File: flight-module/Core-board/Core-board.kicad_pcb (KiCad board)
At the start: 4 copper layers, 127 x 95.2 mm, 28 parts, among them J1 POWER, J10 PCIE, J2 PCIE, J3 XT60-M, J4 PCIE, J5 PCIE, J6 ESP32-DEVKITC-32D, J7 Conn_01x19_Male, J8 PCIE, J9 Conn_01x19_Male, SW1 SW_SPST, U1 AZ1117IH-3.3TRG1, U2 74HC4050D, U3 XTSD04GLGEAG, U4 AZ1117IH-5TRG1

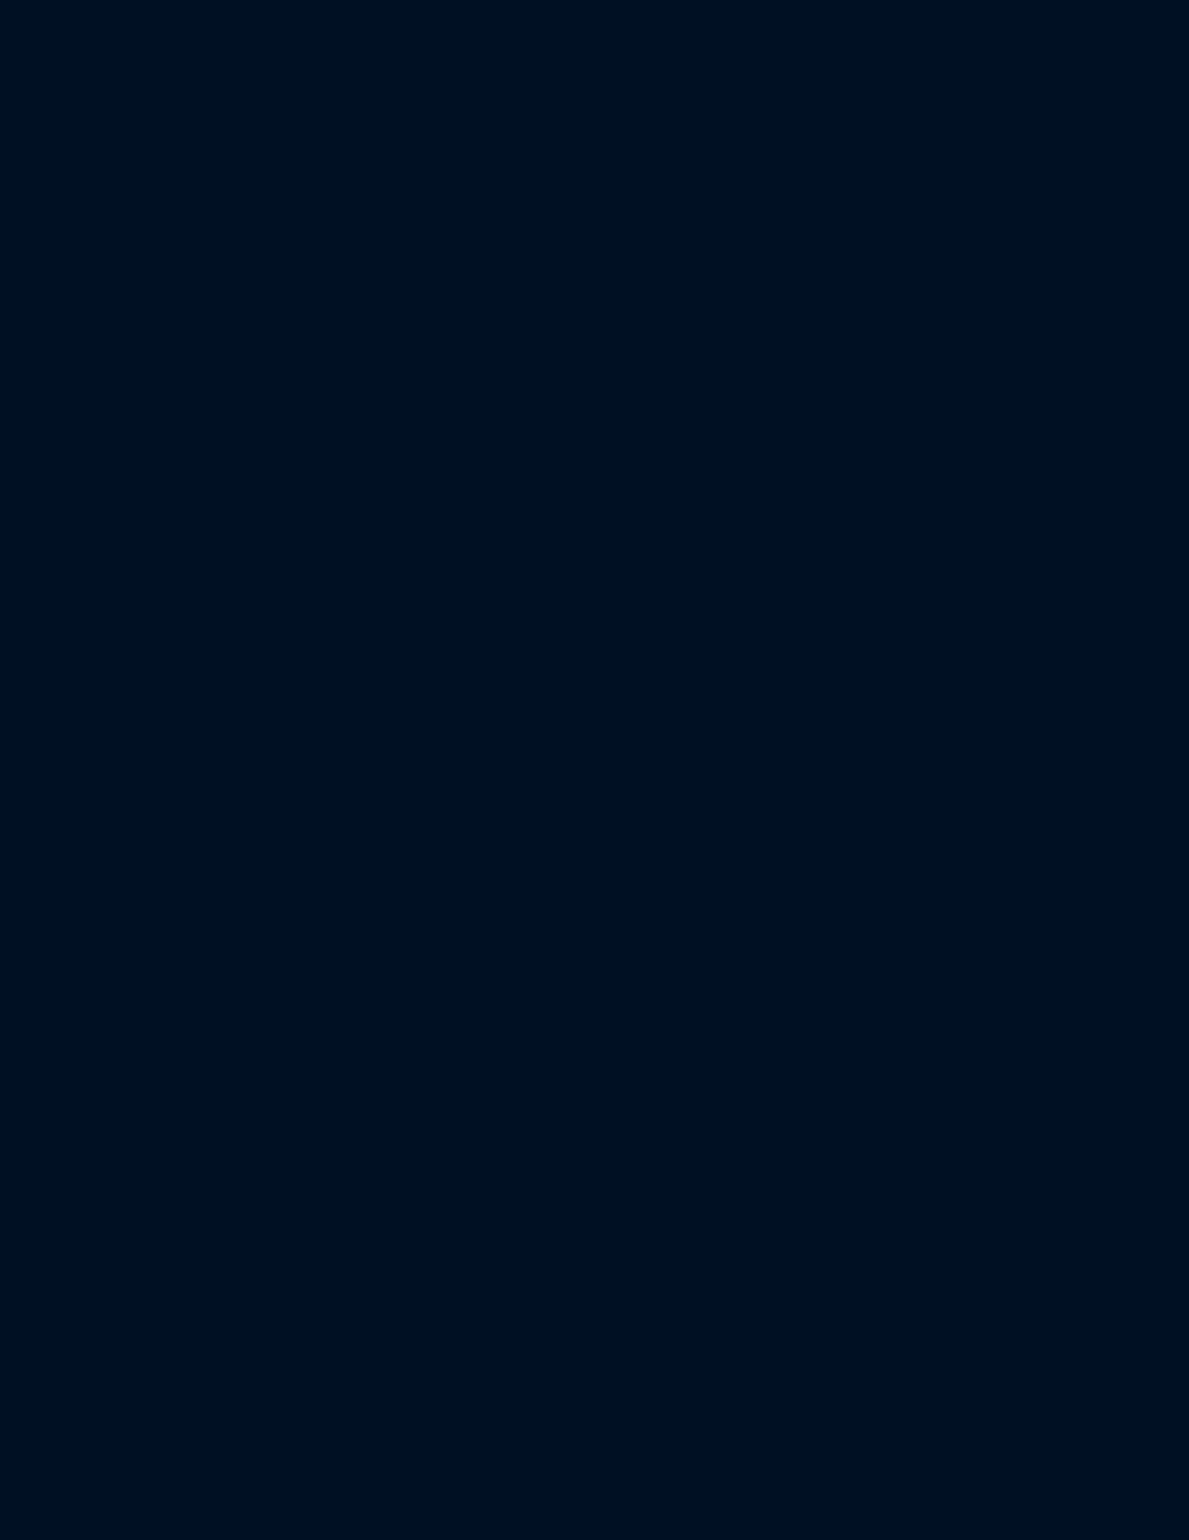
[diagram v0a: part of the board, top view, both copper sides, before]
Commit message: worked on core-board schematic. Not done.
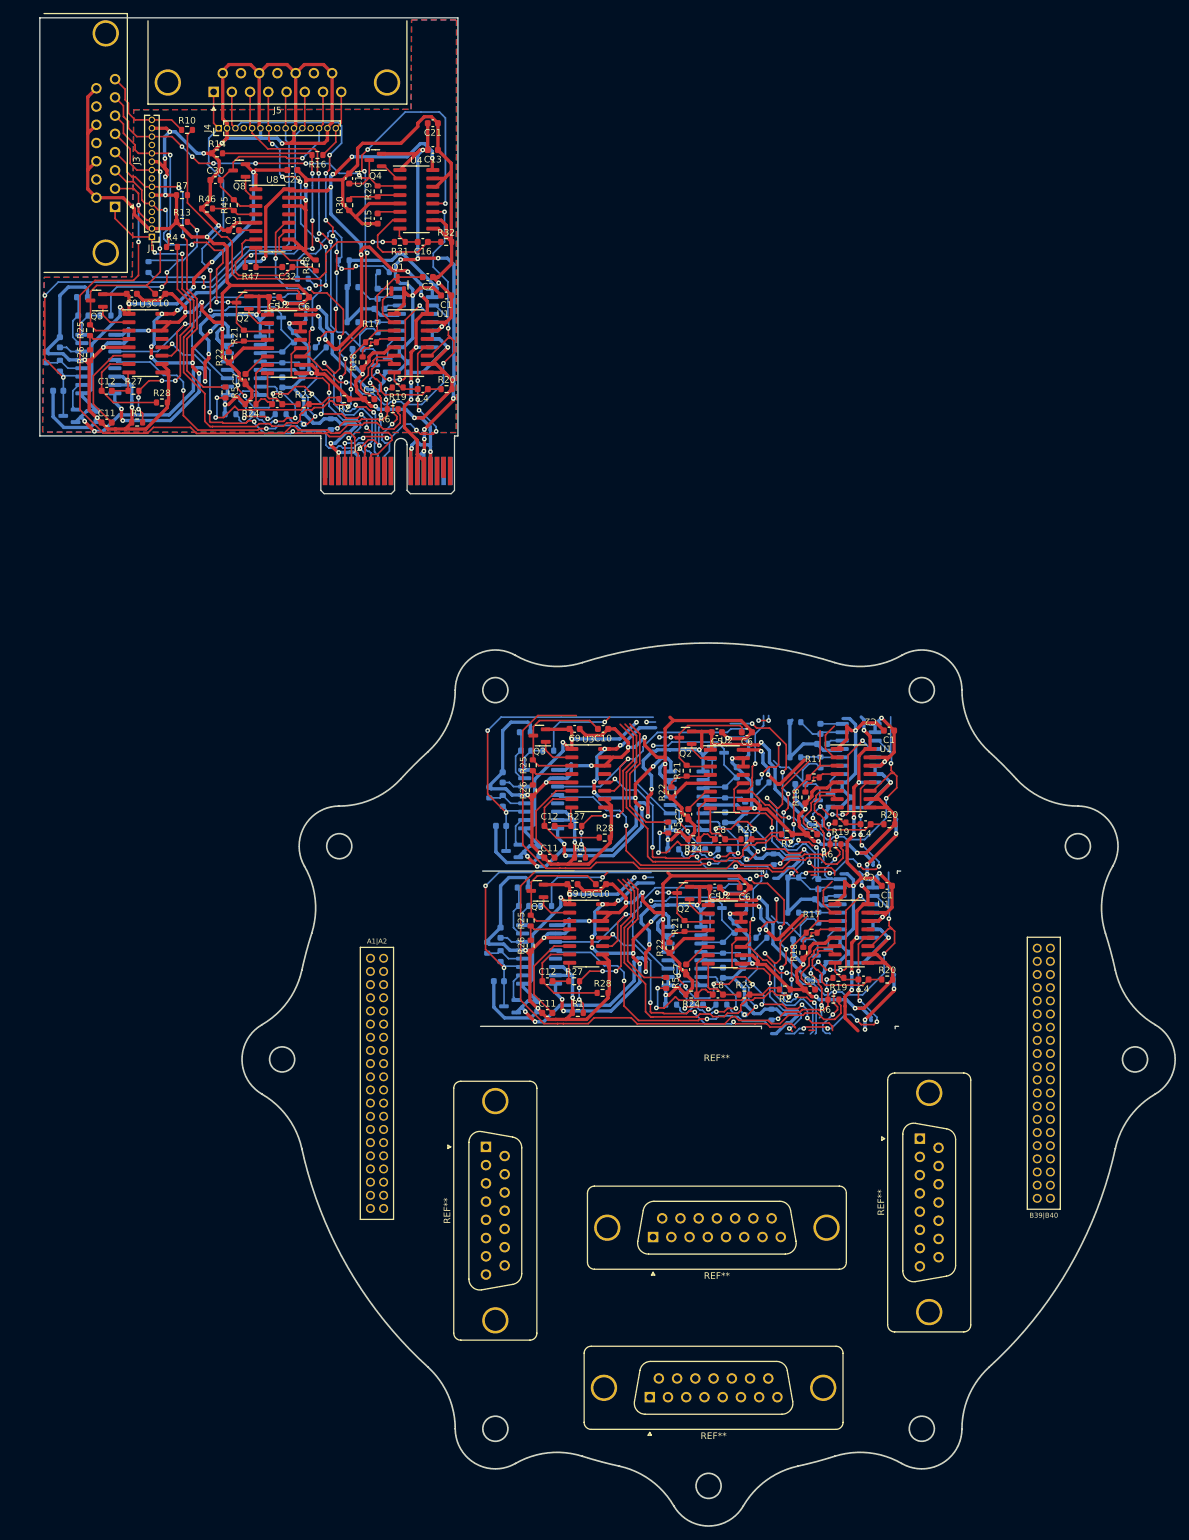
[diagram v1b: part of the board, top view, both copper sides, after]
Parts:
- added C1: 10uF, Capacitor_SMD:C_0603_1608Metric, F.Cu at (521.9, 120.1)
- added C1: 10uF, Capacitor_SMD:C_0603_1608Metric, F.Cu at (454.9, 30.4)
- added C1: 10uF, Capacitor_SMD:C_0603_1608Metric, F.Cu at (522.2, 96.5)
- added C10: 10uF, Capacitor_SMD:C_0603_1608Metric, F.Cu at (478.4, 119.8)
- added C10: 10uF, Capacitor_SMD:C_0603_1608Metric, F.Cu at (411.5, 30.1)
- added C10: 10uF, Capacitor_SMD:C_0603_1608Metric, F.Cu at (478.8, 96.2)
- added C11: 0.1uF, Capacitor_SMD:C_0603_1608Metric, F.Cu at (470.6, 115.8)
- added C11: 0.1uF, Capacitor_SMD:C_0603_1608Metric, F.Cu at (403.4, 49.7)
- added C11: 0.1uF, Capacitor_SMD:C_0603_1608Metric, F.Cu at (470.3, 139.4)
- added C12: 0.1uF, Capacitor_SMD:C_0603_1608Metric, F.Cu at (470.6, 111.0)
- added C12: 0.1uF, Capacitor_SMD:C_0603_1608Metric, F.Cu at (470.3, 134.5)
- added C12: 0.1uF, Capacitor_SMD:C_0603_1608Metric, F.Cu at (403.4, 44.9)
- added C13: 10uF, Capacitor_SMD:C_0603_1608Metric, F.Cu at (452.9, 8.29)
- added C14: 10uF, Capacitor_SMD:C_0603_1608Metric, F.Cu at (440.2, 12.6)
- added C15: 0.1uF, Capacitor_SMD:C_0603_1608Metric, F.Cu at (444.5, 18.7)
- added C16: 0.1uF, Capacitor_SMD:C_0603_1608Metric, F.Cu at (451.4, 22.3)
- added C17: 10uF, Capacitor_SMD:C_0603_1608Metric, B.Cu at (516.4, 107.4)
- added C17: 10uF, Capacitor_SMD:C_0603_1608Metric, B.Cu at (449.1, 41.3)
- added C17: 10uF, Capacitor_SMD:C_0603_1608Metric, B.Cu at (516.0, 131.0)
- added C18: 10uF, Capacitor_SMD:C_0603_1608Metric, B.Cu at (498.8, 126.4)
- added C18: 10uF, Capacitor_SMD:C_0603_1608Metric, B.Cu at (499.1, 102.8)
- added C18: 10uF, Capacitor_SMD:C_0603_1608Metric, B.Cu at (431.8, 36.8)
- added C19: 0.1uF, Capacitor_SMD:C_0603_1608Metric, B.Cu at (497.3, 109.7)
- added C19: 0.1uF, Capacitor_SMD:C_0603_1608Metric, B.Cu at (430.0, 43.6)
- added C19: 0.1uF, Capacitor_SMD:C_0603_1608Metric, B.Cu at (497.0, 133.3)
- added C2: 10uF, Capacitor_SMD:C_0603_1608Metric, F.Cu at (452.1, 27.6)
- added C20: 0.1uF, Capacitor_SMD:C_0603_1608Metric, B.Cu at (493.2, 138.1)
- added C20: 0.1uF, Capacitor_SMD:C_0603_1608Metric, B.Cu at (493.5, 114.5)
- added C20: 0.1uF, Capacitor_SMD:C_0603_1608Metric, B.Cu at (426.2, 48.4)
- added C21: 10uF, Capacitor_SMD:C_0603_1608Metric, F.Cu at (452.9, 4.23)
- added C22: 10uF, Capacitor_SMD:C_0603_1608Metric, B.Cu at (508.4, 128.2)
- added C22: 10uF, Capacitor_SMD:C_0603_1608Metric, B.Cu at (508.7, 104.6)
- added C22: 10uF, Capacitor_SMD:C_0603_1608Metric, B.Cu at (441.5, 38.5)
- added C23: 0.1uF, Capacitor_SMD:C_0603_1608Metric, B.Cu at (511.7, 122.1)
- added C23: 0.1uF, Capacitor_SMD:C_0603_1608Metric, B.Cu at (444.8, 32.4)
- added C23: 0.1uF, Capacitor_SMD:C_0603_1608Metric, B.Cu at (512.0, 98.5)
- added C24: 0.1uF, Capacitor_SMD:C_0603_1608Metric, B.Cu at (511.5, 119.8)
- added C24: 0.1uF, Capacitor_SMD:C_0603_1608Metric, B.Cu at (511.8, 96.2)
- added C24: 0.1uF, Capacitor_SMD:C_0603_1608Metric, B.Cu at (444.5, 30.1)
- added C25: 10uF, Capacitor_SMD:C_0603_1608Metric, B.Cu at (469.1, 114.8)
- added C25: 10uF, Capacitor_SMD:C_0603_1608Metric, B.Cu at (401.9, 48.7)
- added C25: 10uF, Capacitor_SMD:C_0603_1608Metric, B.Cu at (468.8, 138.4)
- added C26: 10uF, Capacitor_SMD:C_0603_1608Metric, B.Cu at (462.9, 134.5)
- added C26: 10uF, Capacitor_SMD:C_0603_1608Metric, B.Cu at (396.0, 44.9)
- added C26: 10uF, Capacitor_SMD:C_0603_1608Metric, B.Cu at (463.3, 111.0)
- added C27: 0.1uF, Capacitor_SMD:C_0603_1608Metric, B.Cu at (396.3, 37.5)
- added C27: 0.1uF, Capacitor_SMD:C_0603_1608Metric, B.Cu at (463.5, 103.6)
- added C27: 0.1uF, Capacitor_SMD:C_0603_1608Metric, B.Cu at (463.2, 127.2)
- added C28: 0.1uF, Capacitor_SMD:C_0603_1608Metric, B.Cu at (466.8, 123.1)
- added C28: 0.1uF, Capacitor_SMD:C_0603_1608Metric, B.Cu at (467.1, 99.5)
- added C28: 0.1uF, Capacitor_SMD:C_0603_1608Metric, B.Cu at (399.8, 33.4)
- added C29: 10uF, Capacitor_SMD:C_0603_1608Metric, F.Cu at (431.6, 11.3)
- added C3: 0.1uF, Capacitor_SMD:C_0603_1608Metric, F.Cu at (443.3, 46.1)
- added C3: 0.1uF, Capacitor_SMD:C_0603_1608Metric, F.Cu at (510.2, 135.8)
- added C3: 0.1uF, Capacitor_SMD:C_0603_1608Metric, F.Cu at (510.5, 112.2)
- added C30: 10uF, Capacitor_SMD:C_0603_1608Metric, F.Cu at (419.9, 12.9)
- added C31: 0.1uF, Capacitor_SMD:C_0603_1608Metric, F.Cu at (422.7, 20.5)
- added C32: 0.1uF, Capacitor_SMD:C_0603_1608Metric, F.Cu at (430.8, 26.1)
- added C4: 0.1uF, Capacitor_SMD:C_0603_1608Metric, F.Cu at (518.6, 110.7)
- added C4: 0.1uF, Capacitor_SMD:C_0603_1608Metric, F.Cu at (451.4, 44.6)
- added C4: 0.1uF, Capacitor_SMD:C_0603_1608Metric, F.Cu at (518.3, 134.3)
- added C5: 10uF, Capacitor_SMD:C_0603_1608Metric, F.Cu at (496.0, 96.7)
- added C5: 10uF, Capacitor_SMD:C_0603_1608Metric, F.Cu at (495.7, 120.3)
- added C5: 10uF, Capacitor_SMD:C_0603_1608Metric, F.Cu at (428.8, 30.6)
- added C6: 10uF, Capacitor_SMD:C_0603_1608Metric, F.Cu at (433.4, 30.6)
- added C6: 10uF, Capacitor_SMD:C_0603_1608Metric, F.Cu at (500.6, 96.7)
- added C6: 10uF, Capacitor_SMD:C_0603_1608Metric, F.Cu at (500.3, 120.3)
- added C7: 0.1uF, Capacitor_SMD:C_0603_1608Metric, F.Cu at (491.4, 132.8)
- added C7: 0.1uF, Capacitor_SMD:C_0603_1608Metric, F.Cu at (424.5, 43.1)
- added C7: 0.1uF, Capacitor_SMD:C_0603_1608Metric, F.Cu at (491.7, 109.2)
- added C8: 0.1uF, Capacitor_SMD:C_0603_1608Metric, F.Cu at (429.3, 46.9)
- added C8: 0.1uF, Capacitor_SMD:C_0603_1608Metric, F.Cu at (496.2, 136.6)
- added C8: 0.1uF, Capacitor_SMD:C_0603_1608Metric, F.Cu at (496.5, 113.0)
- added C9: 10uF, Capacitor_SMD:C_0603_1608Metric, F.Cu at (474.1, 119.8)
- added C9: 10uF, Capacitor_SMD:C_0603_1608Metric, F.Cu at (474.4, 96.2)
- added C9: 10uF, Capacitor_SMD:C_0603_1608Metric, F.Cu at (407.2, 30.1)
- added J1: Testpoints, Connector_PinHeader_1.27mm:PinHeader_1x15_P1.27mm_Vertical, F.Cu at (410.2, 21.5)
- added J2: PCIE-LP-01-01-F-DV-A-TR, Connector_PCBEdge:BUS_PCIexpress_x1, F.Cu at (436.6, 57.0)
- added J3: DB15_Female, DSUB_622-015-260-042:DSUB_622-015-260-042, F.Cu at (404.6, 16.9)
- added J4: Testpoints, Connector_PinHeader_1.27mm:PinHeader_1x15_P1.27mm_Vertical, F.Cu at (420.4, 4.99)
- added J5: DB15_Female, DSUB_622-015-260-042:DSUB_622-015-260-042, F.Cu at (419.6, -0.53)
- added Q1: MMBT4403LT3G, Package_TO_SOT_SMD:SOT-23, F.Cu at (447.6, 28.8)
- added Q2: MMBT4403LT3G, Package_TO_SOT_SMD:SOT-23, F.Cu at (491.0, 121.1)
- added Q2: MMBT4403LT3G, Package_TO_SOT_SMD:SOT-23, F.Cu at (424.0, 31.5)
- added Q2: MMBT4403LT3G, Package_TO_SOT_SMD:SOT-23, F.Cu at (491.3, 97.6)
- added Q3: MMBT4403LT3G, Package_TO_SOT_SMD:SOT-23, F.Cu at (401.9, 31.2)
- added Q3: MMBT4403LT3G, Package_TO_SOT_SMD:SOT-23, F.Cu at (469.1, 97.2)
- added Q3: MMBT4403LT3G, Package_TO_SOT_SMD:SOT-23, F.Cu at (468.8, 120.8)
- added Q4: MMBT4403LT3G, Package_TO_SOT_SMD:SOT-23, F.Cu at (444.2, 9.82)
- added Q5: MMBT4403LT3G, Package_TO_SOT_SMD:SOT-23, B.Cu at (496.2, 99.8)
- added Q5: MMBT4403LT3G, Package_TO_SOT_SMD:SOT-23, B.Cu at (429.0, 33.8)
- added Q5: MMBT4403LT3G, Package_TO_SOT_SMD:SOT-23, B.Cu at (495.9, 123.4)
- added Q6: MMBT4403LT3G, Package_TO_SOT_SMD:SOT-23, B.Cu at (445.1, 41.0)
- added Q6: MMBT4403LT3G, Package_TO_SOT_SMD:SOT-23, B.Cu at (512.4, 107.1)
- added Q6: MMBT4403LT3G, Package_TO_SOT_SMD:SOT-23, B.Cu at (512.0, 130.7)
- added Q7: MMBT4403LT3G, Package_TO_SOT_SMD:SOT-23, B.Cu at (464.6, 138.4)
- added Q7: MMBT4403LT3G, Package_TO_SOT_SMD:SOT-23, B.Cu at (397.7, 48.7)
- added Q7: MMBT4403LT3G, Package_TO_SOT_SMD:SOT-23, B.Cu at (465.0, 114.8)
- added Q8: MMBT4403LT3G, Package_TO_SOT_SMD:SOT-23, F.Cu at (423.5, 11.4)
- added R1: 2kΩ, Resistor_SMD:R_0603_1608Metric, F.Cu at (475.3, 115.8)
- added R1: 2kΩ, Resistor_SMD:R_0603_1608Metric, F.Cu at (474.9, 139.4)
- added R1: 2kΩ, Resistor_SMD:R_0603_1608Metric, F.Cu at (408.0, 49.7)
- added R10: 100kΩ, Resistor_SMD:R_0603_1608Metric, F.Cu at (415.6, 5.25)
- added R11: 100kΩ, Resistor_SMD:R_0603_1608Metric, B.Cu at (433.2, 27.9)
- added R12: 100kΩ, Resistor_SMD:R_0603_1608Metric, B.Cu at (503.1, 104.3)
- added R12: 100kΩ, Resistor_SMD:R_0603_1608Metric, B.Cu at (435.9, 38.3)
- added R12: 100kΩ, Resistor_SMD:R_0603_1608Metric, B.Cu at (502.8, 127.9)
- added R13: 2kΩ, Resistor_SMD:R_0603_1608Metric, F.Cu at (414.8, 19.2)
- added R14: 2kΩ, Resistor_SMD:R_0603_1608Metric, F.Cu at (420.1, 8.80)
- added R15: 100kΩ, Resistor_SMD:R_0603_1608Metric, B.Cu at (409.7, 26.1)
- added R16: 100kΩ, Resistor_SMD:R_0603_1608Metric, F.Cu at (435.4, 9.06)
- added R17: 20kΩ, Resistor_SMD:R_0603_1608Metric, F.Cu at (443.5, 37.5)
- added R17: 20kΩ, Resistor_SMD:R_0603_1608Metric, F.Cu at (510.8, 103.6)
- added R17: 20kΩ, Resistor_SMD:R_0603_1608Metric, F.Cu at (510.4, 127.2)
- added R18: 8.2kΩ, Resistor_SMD:R_0603_1608Metric, F.Cu at (509.5, 106.6)
- added R18: 8.2kΩ, Resistor_SMD:R_0603_1608Metric, F.Cu at (442.2, 40.6)
- added R18: 8.2kΩ, Resistor_SMD:R_0603_1608Metric, F.Cu at (509.2, 130.2)
- added R19: 100Ω, Resistor_SMD:R_0603_1608Metric, F.Cu at (514.8, 110.4)
- added R19: 100Ω, Resistor_SMD:R_0603_1608Metric, F.Cu at (514.5, 134.0)
- added R19: 100Ω, Resistor_SMD:R_0603_1608Metric, F.Cu at (447.6, 44.4)
- added R2: 2kΩ, Resistor_SMD:R_0603_1608Metric, F.Cu at (506.7, 112.2)
- added R2: 2kΩ, Resistor_SMD:R_0603_1608Metric, F.Cu at (439.4, 46.1)
- added R2: 2kΩ, Resistor_SMD:R_0603_1608Metric, F.Cu at (506.4, 135.8)
- added R20: 100Ω, Resistor_SMD:R_0603_1608Metric, F.Cu at (521.9, 134.3)
- added R20: 100Ω, Resistor_SMD:R_0603_1608Metric, F.Cu at (455.0, 44.6)
- added R20: 100Ω, Resistor_SMD:R_0603_1608Metric, F.Cu at (522.2, 110.7)
- added R21: 20kΩ, Resistor_SMD:R_0603_1608Metric, F.Cu at (491.5, 102.6)
- added R21: 20kΩ, Resistor_SMD:R_0603_1608Metric, F.Cu at (491.1, 126.2)
- added R21: 20kΩ, Resistor_SMD:R_0603_1608Metric, F.Cu at (424.2, 36.5)
- added R22: 8.2kΩ, Resistor_SMD:R_0603_1608Metric, F.Cu at (421.9, 39.8)
- added R22: 8.2kΩ, Resistor_SMD:R_0603_1608Metric, F.Cu at (489.2, 105.9)
- added R22: 8.2kΩ, Resistor_SMD:R_0603_1608Metric, F.Cu at (488.9, 129.5)
- added R23: 100Ω, Resistor_SMD:R_0603_1608Metric, F.Cu at (500.2, 136.6)
- added R23: 100Ω, Resistor_SMD:R_0603_1608Metric, F.Cu at (433.3, 46.9)
- added R23: 100Ω, Resistor_SMD:R_0603_1608Metric, F.Cu at (500.5, 113.0)
- added R24: 100Ω, Resistor_SMD:R_0603_1608Metric, F.Cu at (492.2, 136.6)
- added R24: 100Ω, Resistor_SMD:R_0603_1608Metric, F.Cu at (425.2, 46.9)
- added R24: 100Ω, Resistor_SMD:R_0603_1608Metric, F.Cu at (492.5, 113.0)
- added R25: 20kΩ, Resistor_SMD:R_0603_1608Metric, F.Cu at (400.8, 35.7)
- added R25: 20kΩ, Resistor_SMD:R_0603_1608Metric, F.Cu at (468.1, 101.7)
- added R25: 20kΩ, Resistor_SMD:R_0603_1608Metric, F.Cu at (467.8, 125.3)
- added R26: 8.2kΩ, Resistor_SMD:R_0603_1608Metric, F.Cu at (400.8, 39.5)
- added R26: 8.2kΩ, Resistor_SMD:R_0603_1608Metric, F.Cu at (468.1, 105.6)
- added R26: 8.2kΩ, Resistor_SMD:R_0603_1608Metric, F.Cu at (467.8, 129.1)
- added R27: 100Ω, Resistor_SMD:R_0603_1608Metric, F.Cu at (474.4, 134.5)
- added R27: 100Ω, Resistor_SMD:R_0603_1608Metric, F.Cu at (474.7, 111.0)
- added R27: 100Ω, Resistor_SMD:R_0603_1608Metric, F.Cu at (407.4, 44.9)
- added R28: 100Ω, Resistor_SMD:R_0603_1608Metric, F.Cu at (411.8, 46.6)
- added R28: 100Ω, Resistor_SMD:R_0603_1608Metric, F.Cu at (479.0, 112.7)
- added R28: 100Ω, Resistor_SMD:R_0603_1608Metric, F.Cu at (478.7, 136.3)
- added R29: 20kΩ, Resistor_SMD:R_0603_1608Metric, F.Cu at (444.5, 14.6)
- added R3: 2kΩ, Resistor_SMD:R_0603_1608Metric, B.Cu at (437.4, 50.0)
- added R3: 2kΩ, Resistor_SMD:R_0603_1608Metric, B.Cu at (504.7, 116.0)
- added R3: 2kΩ, Resistor_SMD:R_0603_1608Metric, B.Cu at (504.3, 139.6)
- added R30: 8.2kΩ, Resistor_SMD:R_0603_1608Metric, F.Cu at (440.2, 16.7)
- added R31: 100Ω, Resistor_SMD:R_0603_1608Metric, F.Cu at (447.9, 22.3)
- added R32: 100Ω, Resistor_SMD:R_0603_1608Metric, F.Cu at (454.9, 22.3)
- added R33: 20kΩ, Resistor_SMD:R_0603_1608Metric, B.Cu at (497.0, 129.5)
- added R33: 20kΩ, Resistor_SMD:R_0603_1608Metric, B.Cu at (430.0, 39.8)
- added R33: 20kΩ, Resistor_SMD:R_0603_1608Metric, B.Cu at (497.3, 105.9)
- added R34: 8.2kΩ, Resistor_SMD:R_0603_1608Metric, B.Cu at (433.1, 42.1)
- added R34: 8.2kΩ, Resistor_SMD:R_0603_1608Metric, B.Cu at (500.4, 108.2)
- added R34: 8.2kΩ, Resistor_SMD:R_0603_1608Metric, B.Cu at (500.0, 131.7)
- added R35: 100Ω, Resistor_SMD:R_0603_1608Metric, B.Cu at (429.8, 48.4)
- added R35: 100Ω, Resistor_SMD:R_0603_1608Metric, B.Cu at (496.7, 138.1)
- added R35: 100Ω, Resistor_SMD:R_0603_1608Metric, B.Cu at (497.0, 114.5)
- added R36: 100Ω, Resistor_SMD:R_0603_1608Metric, B.Cu at (489.4, 114.5)
- added R36: 100Ω, Resistor_SMD:R_0603_1608Metric, B.Cu at (422.2, 48.4)
- added R36: 100Ω, Resistor_SMD:R_0603_1608Metric, B.Cu at (489.1, 138.1)
- added R37: 20kΩ, Resistor_SMD:R_0603_1608Metric, B.Cu at (444.5, 35.2)
- added R37: 20kΩ, Resistor_SMD:R_0603_1608Metric, B.Cu at (511.5, 124.9)
- added R37: 20kΩ, Resistor_SMD:R_0603_1608Metric, B.Cu at (511.8, 101.3)
- added R38: 8.2kΩ, Resistor_SMD:R_0603_1608Metric, B.Cu at (507.6, 124.1)
- added R38: 8.2kΩ, Resistor_SMD:R_0603_1608Metric, B.Cu at (440.7, 34.5)
- added R38: 8.2kΩ, Resistor_SMD:R_0603_1608Metric, B.Cu at (508.0, 100.5)
- added R39: 100Ω, Resistor_SMD:R_0603_1608Metric, B.Cu at (445.5, 26.8)
- added R4: 100kΩ, Resistor_SMD:R_0603_1608Metric, F.Cu at (413.3, 23.0)
- added R40: 100Ω, Resistor_SMD:R_0603_1608Metric, B.Cu at (507.6, 118.8)
- added R40: 100Ω, Resistor_SMD:R_0603_1608Metric, B.Cu at (440.7, 29.1)
- added R40: 100Ω, Resistor_SMD:R_0603_1608Metric, B.Cu at (508.0, 95.2)
- added R41: 20kΩ, Resistor_SMD:R_0603_1608Metric, B.Cu at (463.2, 130.7)
- added R41: 20kΩ, Resistor_SMD:R_0603_1608Metric, B.Cu at (396.3, 41.1)
- added R41: 20kΩ, Resistor_SMD:R_0603_1608Metric, B.Cu at (463.5, 107.1)
- added R42: 8.2kΩ, Resistor_SMD:R_0603_1608Metric, B.Cu at (461.2, 129.5)
- added R42: 8.2kΩ, Resistor_SMD:R_0603_1608Metric, B.Cu at (461.5, 105.9)
- added R42: 8.2kΩ, Resistor_SMD:R_0603_1608Metric, B.Cu at (394.2, 39.8)
- added R43: 100Ω, Resistor_SMD:R_0603_1608Metric, B.Cu at (470.4, 99.5)
- added R43: 100Ω, Resistor_SMD:R_0603_1608Metric, B.Cu at (470.1, 123.1)
- added R43: 100Ω, Resistor_SMD:R_0603_1608Metric, B.Cu at (403.2, 33.4)
- added R44: 100Ω, Resistor_SMD:R_0603_1608Metric, B.Cu at (399.6, 30.6)
- added R44: 100Ω, Resistor_SMD:R_0603_1608Metric, B.Cu at (466.6, 120.3)
- added R44: 100Ω, Resistor_SMD:R_0603_1608Metric, B.Cu at (466.9, 96.7)
- added R45: 20kΩ, Resistor_SMD:R_0603_1608Metric, F.Cu at (422.7, 16.7)
- added R46: 8.2kΩ, Resistor_SMD:R_0603_1608Metric, F.Cu at (418.6, 17.2)
- added R47: 100Ω, Resistor_SMD:R_0603_1608Metric, F.Cu at (425.2, 26.1)
- added R48: 100Ω, Resistor_SMD:R_0603_1608Metric, F.Cu at (435.1, 25.8)
- added R5: 100kΩ, Resistor_SMD:R_0603_1608Metric, F.Cu at (488.3, 134.8)
- added R5: 100kΩ, Resistor_SMD:R_0603_1608Metric, F.Cu at (488.7, 111.2)
- added R5: 100kΩ, Resistor_SMD:R_0603_1608Metric, F.Cu at (421.4, 45.1)
- added R6: 100kΩ, Resistor_SMD:R_0603_1608Metric, F.Cu at (513.7, 137.3)
- added R6: 100kΩ, Resistor_SMD:R_0603_1608Metric, F.Cu at (446.8, 47.7)
- added R6: 100kΩ, Resistor_SMD:R_0603_1608Metric, F.Cu at (514.1, 113.7)
- added R7: 2kΩ, Resistor_SMD:R_0603_1608Metric, F.Cu at (414.8, 15.2)
- added R8: 2kΩ, Resistor_SMD:R_0603_1608Metric, B.Cu at (439.4, 25.1)
- added R9: 2kΩ, Resistor_SMD:R_0603_1608Metric, B.Cu at (433.3, 49.1)
- added R9: 2kΩ, Resistor_SMD:R_0603_1608Metric, B.Cu at (500.6, 115.2)
- added R9: 2kΩ, Resistor_SMD:R_0603_1608Metric, B.Cu at (500.2, 138.8)
- added REF**: DSUB-15_Female_Vertical_P2.77x2.84mm_MountingHoles, Connector_Dsub:DSUB-15_Female_Vertical_P2.77x2.84mm_MountingHoles, F.Cu at (461.0, 159.7)
- added REF**: DSUB-15_Female_Vertical_P2.77x2.84mm_MountingHoles, Connector_Dsub:DSUB-15_Female_Vertical_P2.77x2.84mm_MountingHoles, F.Cu at (486.4, 173.4)
- added REF**: Stack_Shape, Stack_Shape:Stack_Shape, F.Cu at (495.8, 147.6)
- added REF**: DSUB-15_Female_Vertical_P2.77x2.84mm_MountingHoles, Connector_Dsub:DSUB-15_Female_Vertical_P2.77x2.84mm_MountingHoles, F.Cu at (485.9, 197.7)
- added REF**: DSUB-15_Female_Vertical_P2.77x2.84mm_MountingHoles, Connector_Dsub:DSUB-15_Female_Vertical_P2.77x2.84mm_MountingHoles, F.Cu at (526.9, 158.5)
- added U1: HX711, Package_SO:SOP-16_3.9x9.9mm_P1.27mm, F.Cu at (516.5, 127.3)
- added U1: HX711, Package_SO:SOP-16_3.9x9.9mm_P1.27mm, F.Cu at (516.8, 103.7)
- added U1: HX711, Package_SO:SOP-16_3.9x9.9mm_P1.27mm, F.Cu at (449.6, 37.6)
- added U2: HX711, Package_SO:SOP-16_3.9x9.9mm_P1.27mm, F.Cu at (497.2, 127.4)
- added U2: HX711, Package_SO:SOP-16_3.9x9.9mm_P1.27mm, F.Cu at (497.6, 103.8)
- added U2: HX711, Package_SO:SOP-16_3.9x9.9mm_P1.27mm, F.Cu at (430.3, 37.8)
- added U3: HX711, Package_SO:SOP-16_3.9x9.9mm_P1.27mm, F.Cu at (476.2, 127.3)
- added U3: HX711, Package_SO:SOP-16_3.9x9.9mm_P1.27mm, F.Cu at (476.5, 103.7)
- added U3: HX711, Package_SO:SOP-16_3.9x9.9mm_P1.27mm, F.Cu at (409.3, 37.6)
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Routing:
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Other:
- board size 127 x 95.2 mm -> 310.1 x 163.5 mm
- board text added: "100kΩ"
- board text added: "C2"
- board text added: "MMBT4403LT3G"
- board text added: "PCIE-LP-01-01-F-DV-A-TR"
- board text added: "Q1"

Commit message: Progress on core board.
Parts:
- removed the C1 at (302.2, 132.5)
- removed the C1 at (521.9, 120.1)
- removed the C1 at (454.9, 30.4)
- removed the C1 at (522.2, 96.5)
- removed the C10 at (478.4, 119.8)
- removed the C10 at (411.5, 30.1)
- removed the C10 at (478.8, 96.2)
- removed the C11 at (470.6, 115.8)
- removed the C11 at (403.4, 49.7)
- removed the C11 at (470.3, 139.4)
- removed the C12 at (470.6, 111.0)
- removed the C12 at (470.3, 134.5)
- removed the C12 at (403.4, 44.9)
- removed the C17 at (516.4, 107.4)
- removed the C17 at (449.1, 41.3)
- removed the C17 at (516.0, 131.0)
- removed the C18 at (498.8, 126.4)
- removed the C18 at (499.1, 102.8)
- removed the C18 at (431.8, 36.8)
- removed the C19 at (497.3, 109.7)
- removed the C19 at (430.0, 43.6)
- removed the C19 at (497.0, 133.3)
- removed the C2 at (452.1, 27.6)
- removed the C2 at (306.2, 136.3)
- removed the C20 at (493.2, 138.1)
- removed the C20 at (493.5, 114.5)
- removed the C20 at (426.2, 48.4)
- removed the C22 at (508.4, 128.2)
- removed the C22 at (508.7, 104.6)
- removed the C22 at (441.5, 38.5)
- removed the C23 at (511.7, 122.1)
- removed the C23 at (444.8, 32.4)
- removed the C23 at (512.0, 98.5)
- removed the C24 at (511.5, 119.8)
- removed the C24 at (511.8, 96.2)
- removed the C24 at (444.5, 30.1)
- removed the C25 at (469.1, 114.8)
- removed the C25 at (401.9, 48.7)
- removed the C25 at (468.8, 138.4)
- removed the C26 at (462.9, 134.5)
- removed the C26 at (396.0, 44.9)
- removed the C26 at (463.3, 111.0)
- removed the C27 at (396.3, 37.5)
- removed the C27 at (463.5, 103.6)
- removed the C27 at (463.2, 127.2)
- removed the C28 at (466.8, 123.1)
- removed the C28 at (467.1, 99.5)
- removed the C28 at (399.8, 33.4)
- removed C29, C30: 10uF, Capacitor_SMD:C_0603_1608Metric
- removed the C3 at (301.6, 144.4)
- removed the C3 at (443.3, 46.1)
- removed the C3 at (510.2, 135.8)
- removed the C3 at (510.5, 112.2)
- removed C31, C32: 0.1uF, Capacitor_SMD:C_0603_1608Metric
- removed the C4 at (518.6, 110.7)
- removed the C4 at (451.4, 44.6)
- removed the C4 at (518.3, 134.3)
- removed the C4 at (311.4, 120.1)
- removed the C5 at (305.6, 148.5)
- removed the C5 at (496.0, 96.7)
- removed the C5 at (495.7, 120.3)
- removed the C5 at (428.8, 30.6)
- removed the C6 at (433.4, 30.6)
- removed the C6 at (500.6, 96.7)
- removed the C6 at (500.3, 120.3)
- removed the C7 at (491.4, 132.8)
- removed the C7 at (424.5, 43.1)
- removed the C7 at (491.7, 109.2)
- removed the C8 at (429.3, 46.9)
- removed the C8 at (496.2, 136.6)
- removed the C8 at (496.5, 113.0)
- removed the C9 at (474.1, 119.8)
- removed the C9 at (474.4, 96.2)
- removed the C9 at (407.2, 30.1)
- removed F1, F4: 6A Fuse, Fuse:Fuse_2920_7451Metric
- removed F2, F3: 500mA Fuse, Fuse:Fuse_0603_1608Metric
- removed G***: LOGO, star:star_8x7
- removed the J1 at (410.2, 21.5)
- removed the J1 at (333.0, 144.9)
- removed J10: PCIE, 10018784-10210TLF:AMPHENOL_10018784-10210TLF
- removed the J2 at (436.6, 57.0)
- removed the J2 at (317.2, 70.5)
- removed the J3 at (404.6, 16.9)
- removed the J3 at (332.7, 99.9)
- removed the J4 at (420.4, 4.99)
- removed the J4 at (270.5, 70.5)
- removed the J5 at (419.6, -0.53)
- removed the J5 at (293.9, 70.5)
- removed the Q2 at (491.0, 121.1)
- removed the Q2 at (424.0, 31.5)
- removed the Q2 at (491.3, 97.6)
- removed the Q3 at (401.9, 31.2)
- removed the Q3 at (469.1, 97.2)
- removed the Q3 at (468.8, 120.8)
- removed the Q5 at (496.2, 99.8)
- removed the Q5 at (429.0, 33.8)
- removed the Q5 at (495.9, 123.4)
- removed the Q6 at (445.1, 41.0)
- removed the Q6 at (512.4, 107.1)
- removed the Q6 at (512.0, 130.7)
- removed Q7 (x3), Q8: MMBT4403LT3G, Package_TO_SOT_SMD:SOT-23
- removed the R1 at (475.3, 115.8)
- removed the R1 at (474.9, 139.4)
- removed the R1 at (316.2, 120.1)
- removed the R1 at (408.0, 49.7)
- removed the R12 at (503.1, 104.3)
- removed the R12 at (435.9, 38.3)
- removed the R12 at (502.8, 127.9)
- removed the R17 at (443.5, 37.5)
- removed the R17 at (510.8, 103.6)
- removed the R17 at (510.4, 127.2)
- removed the R18 at (509.5, 106.6)
- removed the R18 at (442.2, 40.6)
- removed the R18 at (509.2, 130.2)
- removed the R19 at (514.8, 110.4)
- removed the R19 at (514.5, 134.0)
- removed the R19 at (447.6, 44.4)
- removed the R2 at (217.7, 137.8)
- removed the R2 at (506.7, 112.2)
- removed the R2 at (439.4, 46.1)
- removed the R2 at (506.4, 135.8)
- removed the R20 at (521.9, 134.3)
- removed the R20 at (455.0, 44.6)
- removed the R20 at (522.2, 110.7)
- removed the R21 at (491.5, 102.6)
- removed the R21 at (491.1, 126.2)
- removed the R21 at (424.2, 36.5)
- removed the R22 at (421.9, 39.8)
- removed the R22 at (489.2, 105.9)
- removed the R22 at (488.9, 129.5)
- removed the R23 at (500.2, 136.6)
- removed the R23 at (433.3, 46.9)
- removed the R23 at (500.5, 113.0)
- removed the R24 at (492.2, 136.6)
- removed the R24 at (425.2, 46.9)
- removed the R24 at (492.5, 113.0)
- removed the R25 at (400.8, 35.7)
- removed the R25 at (468.1, 101.7)
- removed the R25 at (467.8, 125.3)
- removed the R26 at (400.8, 39.5)
- removed the R26 at (468.1, 105.6)
- removed the R26 at (467.8, 129.1)
- removed the R27 at (474.4, 134.5)
- removed the R27 at (474.7, 111.0)
- removed the R27 at (407.4, 44.9)
- removed the R28 at (411.8, 46.6)
- removed the R28 at (479.0, 112.7)
- removed the R28 at (478.7, 136.3)
- removed the R3 at (437.4, 50.0)
- removed the R3 at (504.7, 116.0)
- removed the R3 at (504.3, 139.6)
- removed the R33 at (497.0, 129.5)
- removed the R33 at (430.0, 39.8)
- removed the R33 at (497.3, 105.9)
- removed the R34 at (433.1, 42.1)
- removed the R34 at (500.4, 108.2)
- removed the R34 at (500.0, 131.7)
- removed the R35 at (429.8, 48.4)
- removed the R35 at (496.7, 138.1)
- removed the R35 at (497.0, 114.5)
- removed the R36 at (489.4, 114.5)
- removed the R36 at (422.2, 48.4)
- removed the R36 at (489.1, 138.1)
- removed the R37 at (444.5, 35.2)
- removed the R37 at (511.5, 124.9)
- removed the R37 at (511.8, 101.3)
- removed the R38 at (507.6, 124.1)
- removed the R38 at (440.7, 34.5)
- removed the R38 at (508.0, 100.5)
- removed R39, R40 (x3), R43 (x3), R44 (x3), R47, R48: 100Ω, Resistor_SMD:R_0603_1608Metric
- removed R41 (x3), R45: 20kΩ, Resistor_SMD:R_0603_1608Metric
- removed R42 (x3), R46: 8.2kΩ, Resistor_SMD:R_0603_1608Metric
- removed the R5 at (488.3, 134.8)
- removed the R5 at (488.7, 111.2)
- removed the R5 at (421.4, 45.1)
- removed the R6 at (513.7, 137.3)
- removed the R6 at (446.8, 47.7)
- removed the R6 at (514.1, 113.7)
- removed the R9 at (433.3, 49.1)
- removed the R9 at (500.6, 115.2)
- removed the R9 at (500.2, 138.8)
- removed REF** (x4): DSUB-15_Female_Vertical_P2.77x2.84mm_MountingHoles, Connector_Dsub:DSUB-15_Female_Vertical_P2.77x2.84mm_MountingHoles
- removed REF**: Stack_Shape, Stack_Shape:Stack_Shape
- removed the U1 at (516.5, 127.3)
- removed the U1 at (516.8, 103.7)
- removed the U1 at (449.6, 37.6)
- removed the U1 at (312.1, 132.5)
- removed the U2 at (291.3, 127.1)
- removed the U2 at (497.2, 127.4)
- removed the U2 at (497.6, 103.8)
- removed the U2 at (430.3, 37.8)
- removed the U3 at (291.6, 114.4)
- removed the U3 at (476.2, 127.3)
- removed the U3 at (476.5, 103.7)
- removed the U3 at (409.3, 37.6)
- removed the U4 at (311.6, 144.4)
- removed the U4 at (450.4, 15.8)
- removed the U5 at (424.2, 41.1)
- removed the U5 at (491.5, 107.1)
- removed the U5 at (491.1, 130.7)
- removed the U6 at (517.3, 123.5)
- removed the U6 at (517.6, 99.9)
- removed the U6 at (450.3, 33.8)
- removed the U7 at (469.0, 130.5)
- removed the U7 at (469.4, 106.9)
- removed the U7 at (402.1, 40.8)
- added C1: 10uF, Capacitor_SMD:C_0603_1608Metric, F.Cu at (385.5, 237.9)
- added C10: 1uF, Capacitor_SMD:C_0805_2012Metric_Pad1.18x1.45mm_HandSolder, F.Cu at (251.9, 47.0)
- added C11: 10uF, Capacitor_SMD:C_1206_3216Metric_Pad1.33x1.80mm_HandSolder, F.Cu at (269.4, 52.1)
- added C12: 22uF, Capacitor_SMD:C_0805_2012Metric_Pad1.18x1.45mm_HandSolder, F.Cu at (251.9, 50.0)
- added C17: 10uF, Capacitor_SMD:C_0603_1608Metric, F.Cu at (330.2, 242.0)
- added C18: 10uF, Capacitor_SMD:C_0603_1608Metric, F.Cu at (330.2, 244.5)
- added C19: 0.1uF, Capacitor_SMD:C_0603_1608Metric, F.Cu at (330.2, 247.0)
- added C2: 10uF, Capacitor_SMD:C_0603_1608Metric, F.Cu at (385.5, 240.4)
- added C20: 0.1uF, Capacitor_SMD:C_0603_1608Metric, F.Cu at (330.2, 249.5)
- added C22: 10uF, Capacitor_SMD:C_0603_1608Metric, F.Cu at (331.5, 188.9)
- added C23: 0.1uF, Capacitor_SMD:C_0603_1608Metric, F.Cu at (331.5, 191.4)
- added C24: 0.1uF, Capacitor_SMD:C_0603_1608Metric, F.Cu at (331.5, 193.9)
- added C25: 10uF, Capacitor_SMD:C_0603_1608Metric, F.Cu at (391.1, 145.7)
- added C26: 10uF, Capacitor_SMD:C_0603_1608Metric, F.Cu at (391.1, 148.2)
- added C27: 0.1uF, Capacitor_SMD:C_0603_1608Metric, F.Cu at (391.1, 150.8)
- added C28: 0.1uF, Capacitor_SMD:C_0603_1608Metric, F.Cu at (391.1, 153.3)
- added C3: 0.1uF, Capacitor_SMD:C_0603_1608Metric, F.Cu at (385.5, 242.9)
- added C4: 0.1uF, Capacitor_SMD:C_0603_1608Metric, F.Cu at (385.5, 245.4)
- added C5: 10uF, Capacitor_SMD:C_0603_1608Metric, F.Cu at (116.0, 114.7)
- added C6: 10uF, Capacitor_SMD:C_0603_1608Metric, F.Cu at (120.9, 111.1)
- added C7: 0.1uF, Capacitor_SMD:C_0603_1608Metric, F.Cu at (116.6, 123.5)
- added C8: 0.1uF, Capacitor_SMD:C_0603_1608Metric, F.Cu at (116.6, 119.8)
- added C9: 1uF, Capacitor_SMD:C_0805_2012Metric_Pad1.18x1.45mm_HandSolder, F.Cu at (251.9, 44.0)
- added D2: D_Schottky, Diode_SMD:D_SOD-128, F.Cu at (284.3, 49.0)
- added D3: GREEN, LED_SMD:LED_1206_3216Metric_Pad1.42x1.75mm_HandSolder, F.Cu at (283.6, 52.7)
- added J1: Stack_Shape, Stack_Shape:Stack_Shape, F.Cu at (130.7, 91.6)
- added J2: Conn_01x03_Pin, Connector_PinHeader_2.54mm:PinHeader_1x03_P2.54mm_Vertical, F.Cu at (398.4, 238.9)
- added J3: USB_B_Micro, Connector_USB:USB_Micro-B_Amphenol_10103594-0001LF_Horizontal, F.Cu at (271.2, 46.4)
- added J4: Conn_01x06_Pin, Connector_PinHeader_2.54mm:PinHeader_1x06_P2.54mm_Vertical, F.Cu at (192.4, 12.4)
- added J5: Conn_01x03_Pin, Connector_PinHeader_2.54mm:PinHeader_1x03_P2.54mm_Vertical, F.Cu at (106.7, 112.6)
- added Q2: MMBT4403LT3G, Package_TO_SOT_SMD:SOT-23, F.Cu at (115.5, 111.0)
- added Q3: MMBT4403LT3G, Package_TO_SOT_SMD:SOT-23, F.Cu at (391.6, 209.8)
- added Q5: MMBT4403LT3G, Package_TO_SOT_SMD:SOT-23, F.Cu at (335.9, 198.8)
- added Q6: MMBT4403LT3G, Package_TO_SOT_SMD:SOT-23, F.Cu at (395.5, 158.2)
- added R1: 100kΩ, Resistor_SMD:R_0603_1608Metric, F.Cu at (106.2, 124.3)
- added R12: 2kΩ, Resistor_SMD:R_0603_1608Metric, F.Cu at (389.1, 266.6)
- added R17: 100Ω, Resistor_SMD:R_0603_1608Metric, F.Cu at (113.1, 124.3)
- added R18: 100Ω, Resistor_SMD:R_0603_1608Metric, F.Cu at (113.1, 121.8)
- added R19: 20kΩ, Resistor_SMD:R_0603_1608Metric, F.Cu at (115.9, 116.9)
- added R2: 100kΩ, Resistor_SMD:R_0603_1608Metric, F.Cu at (322.8, 236.7)
- added R20: 8.2kΩ, Resistor_SMD:R_0603_1608Metric, F.Cu at (112.4, 116.0)
- added R21: 10k, Resistor_SMD:R_0805_2012Metric_Pad1.20x1.40mm_HandSolder, F.Cu at (278.2, 44.0)
- added R22: 300, Resistor_SMD:R_0805_2012Metric_Pad1.20x1.40mm_HandSolder, F.Cu at (278.2, 46.9)
- added R23: 100Ω, Resistor_SMD:R_0603_1608Metric, F.Cu at (387.1, 207.4)
- added R24: 100Ω, Resistor_SMD:R_0603_1608Metric, F.Cu at (387.1, 209.9)
- added R25: 20kΩ, Resistor_SMD:R_0603_1608Metric, F.Cu at (387.1, 212.5)
- added R26: 8.2kΩ, Resistor_SMD:R_0603_1608Metric, F.Cu at (387.1, 215.0)
- added R27: 100Ω, Resistor_SMD:R_0603_1608Metric, F.Cu at (330.2, 252.0)
- added R28: 100Ω, Resistor_SMD:R_0603_1608Metric, F.Cu at (330.2, 254.5)
- added R3: 100kΩ, Resistor_SMD:R_0603_1608Metric, F.Cu at (326.1, 200.7)
- added R33: 20kΩ, Resistor_SMD:R_0603_1608Metric, F.Cu at (331.5, 201.5)
- added R34: 8.2kΩ, Resistor_SMD:R_0603_1608Metric, F.Cu at (331.5, 204.0)
- added R35: 100Ω, Resistor_SMD:R_0603_1608Metric, F.Cu at (391.1, 155.8)
- added R36: 100Ω, Resistor_SMD:R_0603_1608Metric, F.Cu at (391.1, 158.3)
- added R37: 20kΩ, Resistor_SMD:R_0603_1608Metric, F.Cu at (391.1, 160.8)
- added R38: 8.2kΩ, Resistor_SMD:R_0603_1608Metric, F.Cu at (391.1, 163.3)
- added R5: 2kΩ, Resistor_SMD:R_0603_1608Metric, F.Cu at (326.8, 234.1)
- added R6: 2kΩ, Resistor_SMD:R_0603_1608Metric, F.Cu at (326.1, 196.5)
- added R9: 100kΩ, Resistor_SMD:R_0603_1608Metric, F.Cu at (383.2, 267.0)
- added SW2: SW_MEC_5E, Button_Switch_SMD:SW_SPST_TL3305A, F.Cu at (244.3, 51.5)
- added U1: HX711, Package_SO:SOP-16_3.9x9.9mm_P1.27mm, F.Cu at (122.8, 118.7)
- added U10: ESP32-S3-WROOM-1-N16R2, RF_Module:ESP32-S3-WROOM-1, F.Cu at (256.2, 20.0)
- added U2: HX711, Package_SO:SOP-16_3.9x9.9mm_P1.27mm, F.Cu at (398.6, 139.0)
- added U3: HX711, Package_SO:SOP-16_3.9x9.9mm_P1.27mm, F.Cu at (346.3, 201.7)
- added U4: HX711, Package_SO:SOP-16_3.9x9.9mm_P1.27mm, F.Cu at (393.9, 189.4)
- added U5: HX711, Package_SO:SOP-16_3.9x9.9mm_P1.27mm, F.Cu at (338.4, 237.4)
- added U6: HX711, Package_SO:SOP-16_3.9x9.9mm_P1.27mm, F.Cu at (402.4, 254.5)
- added U7: XTSD04GLGEAG, XTSD04GLGEAG:SON127P600X800X95-8N, F.Cu at (197.1, 34.2)
- added U9: AZ1084-3.3, Package_TO_SOT_SMD:TO-252-2, F.Cu at (279.1, 25.6)
- D1: value D_Small -> PESD12VL2BT; footprint Diode_SMD:D_0603_1608Metric -> Package_TO_SOT_SMD:SOT-23
- J6: value ESP32-DEVKITC-32D -> Conn_01x03_Pin; footprint Ellie_Project_Footprints:MODULE_ESP32-DEVKITC-32D -> Connector_PinHeader_2.54mm:PinHeader_1x03_P2.54mm_Vertical
- J7, J9: value Conn_01x19_Male -> Conn_01x03_Pin; footprint Connector_PinHeader_2.54mm:PinHeader_1x19_P2.54mm_Vertical -> Connector_PinHeader_2.54mm:PinHeader_1x03_P2.54mm_Vertical
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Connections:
- C13 pad 2: +5V -> /HX4_E+
- C14 pad 2: (no net) -> +5V
- C15 pad 1: GND -> Net-(U4-INA-)
- C15 pad 2: (no net) -> Net-(U4-INA+)
- C16 pad 1: (no net) -> GND
- C16 pad 2: (no net) -> Net-(U4-VBG)
- C21 pad 2: +5V -> /HX3_E+
- D1 pad 1: Net-(D1-Pad1) -> /ESP32-S3-WROOM-1-Breakout/USB_D+
- D1 pad 2: GND -> /ESP32-S3-WROOM-1-Breakout/USB_D-
- J6 pad 1: 3.3V -> /HX4_E+
- J6 pad 2: EN -> GND
- J6 pad 3: HX1 -> /HX711 4/A+
- J7 pad 1: +5V -> /HX5_E+
- J7 pad 2: unconnected-(J7-Pad2) -> GND
- J7 pad 3: unconnected-(J7-Pad3) -> /HX711 5/A+
- J9 pad 1: GND -> /HX2_E+
- J9 pad 2: SD, TC MISO -> GND
- J9 pad 3: MOS SCL -> /HX711 2/A+
- Q1 pad 1: (no net) -> Net-(Q1-B)
- Q1 pad 3: (no net) -> /HX6_E+
- Q4 pad 1: (no net) -> Net-(Q4-B)
- Q4 pad 3: (no net) -> /HX5_E+
- R10 pad 1: (no net) -> GND
- R10 pad 2: (no net) -> /HX711 2/A+
- R11 pad 1: (no net) -> GND
- R11 pad 2: (no net) -> /HX711 4/A+
- R13 pad 1: GND -> Net-(U6-INA+)
- R13 pad 2: (no net) -> /HX711 6/A+
- R14 pad 1: GND -> Net-(U6-INA-)
- R14 pad 2: (no net) -> GND
- R15 pad 1: (no net) -> Net-(U6-VFB)
- R15 pad 2: (no net) -> /HX6_E+
- R16 pad 1: (no net) -> GND
- R16 pad 2: (no net) -> Net-(U6-VFB)
- R29 pad 1: (no net) -> Net-(U5-VFB)
- R29 pad 2: (no net) -> /HX5_E+
- R30 pad 2: (no net) -> Net-(U5-VFB)
- R31 pad 1: (no net) -> Net-(U3-INA+)
- R31 pad 2: (no net) -> /HX711 3/A+
- R32 pad 1: (no net) -> Net-(U3-INA-)
- R4 pad 1: (no net) -> GND
- R4 pad 2: (no net) -> /HX711 1/A+
- R7 pad 1: GND -> /HX2_A+
- R7 pad 2: (no net) -> /HX711 2/A+
- R8 pad 1: GND -> /HX4_A+
- R8 pad 2: (no net) -> /HX711 4/A+
- SW1 pad 1: EN -> GND
- SW1 pad 2: Net-(R2-Pad1) -> /ESP32-S3-WROOM-1-Breakout/BOOT
- U8 pad 1: +5V -> +3.3V
- U8 pad 10: GND -> unconnected-(U8-4Y-Pad10)
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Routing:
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- added copper zone on In2.Cu, net +5V
- added copper zone on In1.Cu, net GND
- removed copper zone on B.Cu, net GND
- removed copper zone on F.Cu, net GND
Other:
- board size 310.1 x 163.5 mm -> 141.7 x 134.1 mm
- board text removed: "+"
- board text removed: "-"
- board text removed: "100kΩ"
- board text removed: "3V3"
- board text removed: "A1"
- board text removed: "B1"
- board text removed: "Banana plug"
- board text removed: "C2"
- board text removed: "Designed by: Khai Sam"
- board text removed: "EN"
- board text removed: "ESP32-DEVKITC-V4"
- board text removed: "GND"
- board text removed: "Ground DAQ 2 LE2 Hotfire 2023"
- board text removed: "HX CLK"
- board text removed: "HX1 DT"
- board text removed: "HX2 DT"
- board text removed: "HX3 DT"
- board text removed: "HX4 DT"
- board text removed: "HX5 DT"
- board text removed: "HX6 DT"
- board text removed: "HX7 DT"
- board text removed: "HX8 DT"
- board text removed: "I2C SCL"
- board text removed: "I2C SDA"
- board text removed: "MMBT4403LT3G"
- board text removed: "PCIE-LP-01-01-F-DV-A-TR"
- board text removed: "PERIPHERAL 1"
- board text removed: "PERIPHERAL 2"
- board text removed: "PERIPHERAL 3"
- board text removed: "PERIPHERAL 4"
- board text removed: "PERIPHERAL 5"
- board text removed: "Q1"
- board text removed: "SD CLK"
- board text removed: "SD CS"
- board text removed: "SD MISO"
- board text removed: "SD MOSI"
- board text removed: "TC CLK"
- board text removed: "TC MISO"
- board text removed: "TC1 CS"
- board text removed: "TC2 CS"
- board text removed: "TC3 CS"
- board text removed: "TC4 CS"
- board text removed: "This side up"
- board text removed: "Wrong side"
- board text removed: "XT-60"
